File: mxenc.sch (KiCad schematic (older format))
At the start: 28 parts, among them J4 Conn_01x06, J6 Conn_01x06, J8 Conn_01x06 DNP, SW1 SW_Push, SW2 SW_Push, U1 IMX8MM, U10 24LC16, Y2 Crystal_GND24

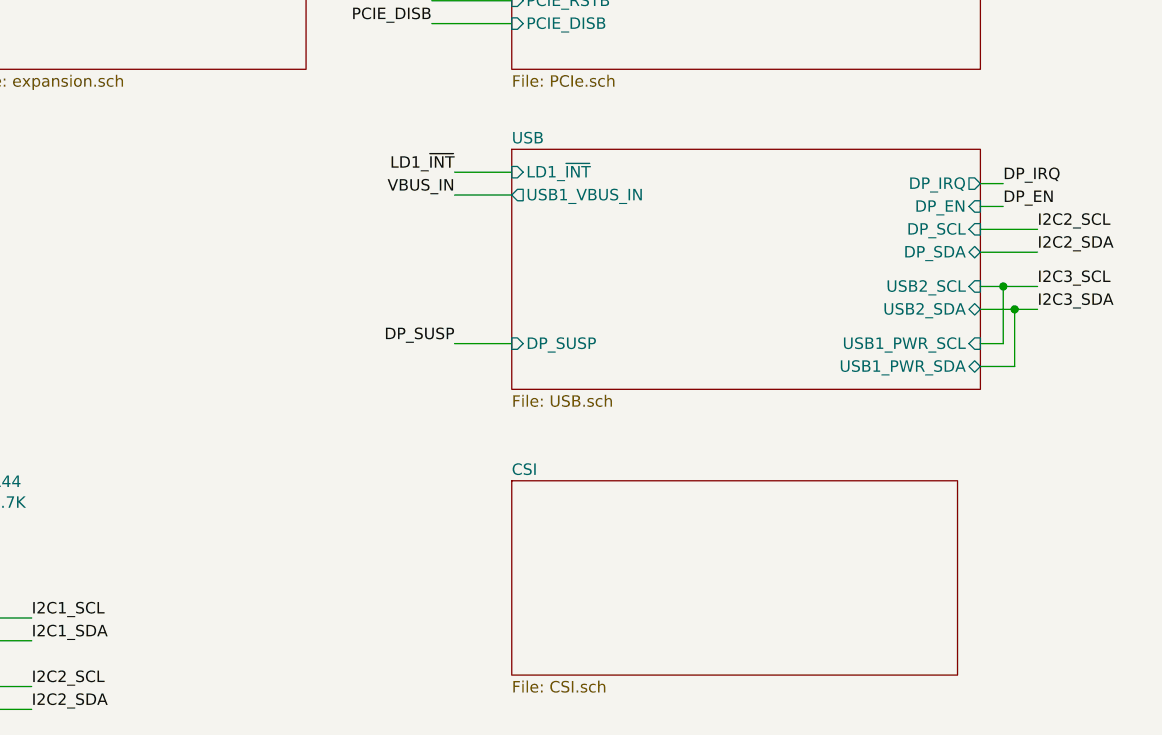
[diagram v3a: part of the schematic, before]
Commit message: UIM and USB routing for PCIE to expansion
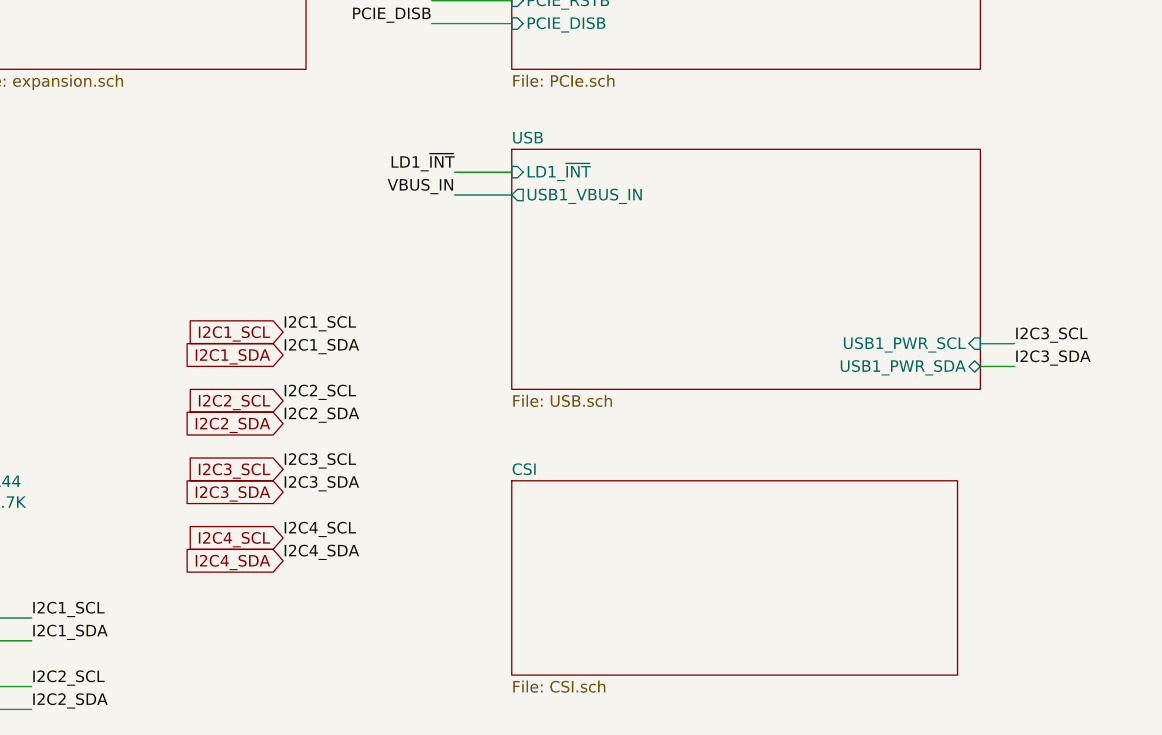
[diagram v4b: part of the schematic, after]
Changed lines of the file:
@@
-$EndSheet
-$Sheet
-S 13350 6750 2050 1050
-U 5D6742B7
-F0 "USB" 50
-F1 "USB.sch" 50
-F2 "LD1_~INT" I L 13350 6850 50
-F3 "USB1_VBUS_IN" O L 13350 6950 50
-F4 "DP_IRQ" O R 15400 6900 50
-F5 "DP_EN" I R 15400 7000 50
-F6 "DP_SCL" I R 15400 7100 50
-F7 "DP_SDA" B R 15400 7200 50
-F8 "USB2_SCL" I R 15400 7350 50
-F9 "USB2_SDA" B R 15400 7450 50
-F10 "USB1_PWR_SDA" B R 15400 7700 50
-F11 "USB1_PWR_SCL" I R 15400 7600 50
-F12 "DP_SUSP" I L 13350 7600 50
 $EndSheet
 $Sheet
@@
 Wire Wire Line
 	13100 6850 13350 6850
-Text Label 15500 7000 0    50   ~ 0
-DP_EN
-Wire Wire Line
-	15500 7000 15400 7000
-Text Label 15500 6900 0    50   ~ 0
-DP_IRQ
-Wire Wire Line
-	15500 6900 15400 6900
 Text Label 13000 5850 2    50   ~ 0
 I2C3_SDA
@@
 Text Label 1700 3350 0    50   ~ 0
 I2C2_SDA
-Text Label 15650 7350 0    50   ~ 0
+Text Label 15550 7600 0    50   ~ 0
 I2C3_SCL
-Text Label 15650 7450 0    50   ~ 0
-I2C3_SDA
-Wire Wire Line
-	15500 7350 15400 7350
-Wire Wire Line
-	15500 7350 15500 7600
-Wire Wire Line
-	15500 7600 15400 7600
-Wire Wire Line
-	15550 7450 15400 7450
-Wire Wire Line
-	15550 7450 15550 7700
+Wire Wire Line
+	15550 7600 15400 7600
 Wire Wire Line
 	15550 7700 15400 7700
-Text Label 13100 7600 2    50   ~ 0
-DP_SUSP
-Wire Wire Line
-	13100 7600 13350 7600
 Wire Wire Line
 	10600 1450 11000 1450
@@
 Text Notes 6200 3350 0    35   ~ 0
 WDOG - input, internal pull-up\nnINT - input, internal pull-up\nVSEL - output, 1.8v push-pull
-Wire Wire Line
-	15400 7100 15650 7100
-Wire Wire Line
-	15400 7200 15650 7200
-Wire Wire Line
-	15650 7350 15500 7350
-Connection ~ 15500 7350
-Wire Wire Line
-	15550 7450 15650 7450
-Connection ~ 15550 7450
 $Comp
 L mxenc:VDD_3V3 #PWR0142
@@
 	10600 7850 10600 7950
 Connection ~ 10600 7950
-Text Label 15650 7100 0    50   ~ 0
-I2C2_SCL
-Text Label 15650 7200 0    50   ~ 0
-I2C2_SDA
 $Comp
 L mxenc:GG_LOGO L8
@@
 ECSPI1_SS0
 $Comp
-L power:GND #PWR?
+L power:GND #PWR0217
 U 1 1 5F2A80D8
 P 2400 1450
-F 0 "#PWR?" H 2400 1200 50  0001 C CNN
+F 0 "#PWR0217" H 2400 1200 50  0001 C CNN
 F 1 "GND" H 2405 1277 50  0000 C CNN
 F 2 "" H 2400 1450 50  0001 C CNN
@@
 $EndComp
 $Comp
-L power:GND #PWR?
+L power:GND #PWR0218
 U 1 1 5F2A97FE
 P 3850 1450
-F 0 "#PWR?" H 3850 1200 50  0001 C CNN
+F 0 "#PWR0218" H 3850 1200 50  0001 C CNN
 F 1 "GND" H 3855 1277 50  0000 C CNN
 F 2 "" H 3850 1450 50  0001 C CNN
@@
 	1    0    0    -1
 $EndComp
+$Sheet
+S 13350 6750 2050 1050
+U 5D6742B7
+F0 "USB" 50
+F1 "USB.sch" 50
+F2 "LD1_~INT" I L 13350 6850 50
+F3 "USB1_VBUS_IN" O L 13350 6950 50
+F10 "USB1_PWR_SDA" B R 15400 7700 50
+F11 "USB1_PWR_SCL" I R 15400 7600 50
+$EndSheet
+Text Label 15550 7700 0    50   ~ 0
+I2C3_SDA
+Text Label 12350 8550 0    50   ~ 0
+I2C4_SDA
+Text Label 12350 8450 0    50   ~ 0
+I2C4_SCL
+Text Label 12350 8250 0    50   ~ 0
+I2C3_SDA
+Text Label 12350 8150 0    50   ~ 0
+I2C3_SCL
+Text Label 12350 7950 0    50   ~ 0
+I2C2_SDA
+Text Label 12350 7850 0    50   ~ 0
+I2C2_SCL
+Text Label 12350 7650 0    50   ~ 0
+I2C1_SDA
+Text Label 12350 7550 0    50   ~ 0
+I2C1_SCL
+Text GLabel 12350 7550 0    50   Input ~ 0
+I2C1_SCL
+Text GLabel 12350 7650 0    50   Input ~ 0
+I2C1_SDA
+Text GLabel 12350 7950 0    50   Input ~ 0
+I2C2_SDA
+Text GLabel 12350 8250 0    50   Input ~ 0
+I2C3_SDA
+Text GLabel 12350 8550 0    50   Input ~ 0
+I2C4_SDA
+Text GLabel 12350 7850 0    50   Input ~ 0
+I2C2_SCL
+Text GLabel 12350 8150 0    50   Input ~ 0
+I2C3_SCL
+Text GLabel 12350 8450 0    50   Input ~ 0
+I2C4_SCL
 $EndSCHEMATC

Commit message: Finish remaining routing
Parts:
- removed J8: Conn_01x06 DNP, Connector_PinHeader_2.54mm:PinHeader_1x06_P2.54mm_Horizontal, symbol Connector_Generic:Conn_01x06
- added J8: Conn_01x04_MountingPin, Connector_JST:JST_SH_SM04B-SRSS-TB_1x04-1MP_P1.00mm_Horizontal, symbol Connector_Generic_MountingPin:Conn_01x04_MountingPin
- added LOGO1: Logo_Open_Hardware_Small, Symbol:OSHW-Logo_5.7x6mm_SilkScreen, symbol Graphic:Logo_Open_Hardware_Small
- added R23, R38: 10K, Resistor_SMD:R_0201_0603Metric, symbol Device:R
- J4, J6: footprint Connector_JST:JST_GH_SM06B-GHS-TB_1x06-1MP_P1.25mm_Horizontal -> Connector_JST:JST_SH_SM06B-SRSS-TB_1x06-1MP_P1.00mm_Horizontal; symbol mxenc:JST-GH-6 -> Connector_Generic_MountingPin:Conn_01x06_MountingPin; Part SM06B-GHS-TB(LF)(SN) -> SM06B-SRSS-TB(LF)(SN); Vendorpart 455-1568-1-ND -> 455-1806-1-ND
- SW1, SW2: footprint mxenc:SW_SPST_EVQP7C -> mxenc:SW_SPST_EVQP7A
- U10: value 24LC16 -> 24C32; Mfgr Microchip -> ST; Part 24LC16B-I/MC -> M24C32-FMC6TG; Vendorpart 24LC16B-I/MC-ND -> 497-15757-1-ND
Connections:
- net VDD_5V is gone; now on net NVCC_3V3: J4.1 (Pin_1), J6.1 (Pin_1)
- net GND: now also J8.1 (Pin_1), J8.MP (MountPin), R38.1
- net I2C2_SCL: no longer U10.6 (SCL)
- net I2C2_SDA: no longer U10.5 (SDA)
- net I2C3_SCL: now also U10.6 (SCL)
- net I2C3_SDA: now also U10.5 (SDA)
- net I2C4_SCL: now also J8.4 (Pin_4)
- net I2C4_SDA: now also J8.3 (Pin_3)
- net JTAG_TRST_B: now also R23.1
- net UART1_CTS_B: no longer J6.4 (Pin_4)
- net UART1_RTS_B: no longer J6.5 (Pin_5)
- net UART1_RX: no longer J6.2 (Pin_2)
- net UART1_TX: no longer J6.3 (Pin_3)
- net VDD_1V8: now also R23.2; no longer U10.8 (VCC)
- net UART4_RX: now reaches U1.F19 (UART4_RXD/GPIO5[28])
- net UART4_RX: now also J6.2 (Pin_2)
- net NVCC_3V3: now reaches U10.1 (A0)
- net NVCC_3V3: now also U10.2 (A1), U10.3 (A2), U10.8 (VCC), J8.2 (Pin_2)
- net JTAG_MOD: no longer names the net of U1.D27 (JTAG_MOD)
- net JTAG_MOD: now also R38.2
- net LD1_~INT renamed UART4_TX
- net UART4_TX: now also J6.3 (Pin_3)
- new net UART4_CTS_B: J6.4 (Pin_4)
- new net UART4_RTS_B: J6.5 (Pin_5)
- no-connect marks 19 -> 14
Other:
- note added: "7-bit addr: 0x57/0x5F"
- note added: "CONSOLE (Pixhawk debug JST-SH)"
- note added: "I2C (QWIIC JST-SH)"
- note added: "UART1 (Pixhawk debug JST-SH)"
- note removed: "CONSOLE (0.1" connector)"
- note removed: "CONSOLE (JST connector)"
- note removed: "UART1 (JST connector)"
- moved on the sheet: L8

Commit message: wip more uart routing
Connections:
- net UART1_RX: now also U1.E14 (UART1_RXD); no longer U1.AB22 (SAI2_RXC/GPIO4[22]/UART1_RX)
- net UART1_TX: now also U1.F13 (UART1_TXD); no longer U1.AC19 (SAI2_RXFS/GPIO4[21]/UART1_TX)
- net UART2_RX: now also U1.F15 (UART2_RXD)
- net UART2_TX: now also U1.E15 (UART2_TXD)
- net UART3_TX: now reaches U1.D18 (UART3_TXD)
- net UART3_RX: now reaches U1.E18 (UART3_RXD)
- net GPIO1[11]: now reaches U1.AC10 (GPIO1_IO11)
- net GPIO1[9]: now reaches U1.AF10 (GPIO1_IO09)
- net UART1_CTS_B: no longer names the net of U1.AD23 (SAI2_TXFS/GPIO4[24]/UART1_CTS_B)
- net UART1_RTS_B: no longer names the net of U1.AC24 (SAI2_RXD0/GPIO4[23]/UART1_RTS_B)
- net USB2_OC renamed GPIO1[15]
- net USB2_PWR_EN renamed GPIO1[14]
- no-connect marks 14 -> 11
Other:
- note added: "A53 debug / UART2 (JST-SH)"
- note added: "M4 debug / UART4 (JST-SH)"
- note added: "QWIIC / I2C4 (JST-SH)"
- note removed: "CONSOLE (Pixhawk debug JST-SH)"
- note removed: "I2C (QWIIC JST-SH)"
- note removed: "UART1 (Pixhawk debug JST-SH)"
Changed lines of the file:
@@
 	1    0    0    -1
 $EndComp
-Wire Wire Line
-	6150 4900 6400 4900
-Wire Wire Line
-	6150 5000 6400 5000
 $Comp
 L mxenc:VDD_1V8 #PWR0246
@@
 Text Label 6450 1700 2    50   ~ 0
 LED_B
-Text Label 7900 2400 2    50   ~ 0
+Text Label 7300 9200 2    50   ~ 0
 UART2_TX
-Text Label 7900 2500 2    50   ~ 0
+Text Label 7300 9100 2    50   ~ 0
 UART2_RX
 Text Label 7900 2600 2    50   ~ 0
@@
 Text Label 7900 2700 2    50   ~ 0
 UART2_CTS_B
-Text Label 7900 3150 2    50   ~ 0
-UART1_TX
-Text Label 7900 3050 2    50   ~ 0
-UART1_RX
-Text Label 7900 2950 2    50   ~ 0
-UART1_RTS_B
-Text Label 7900 2850 2    50   ~ 0
-UART1_CTS_B
 Text Label 3500 1400 2    50   ~ 0
 UART2_TX
@@
 $EndSheet
 Text Notes 3150 2200 0    50   ~ 0
-CONSOLE (Pixhawk debug JST-SH)
+A53 debug / UART2 (JST-SH)
 Text Notes 1650 2200 0    50   ~ 0
-UART1 (Pixhawk debug JST-SH)
+M4 debug / UART4 (JST-SH)
 Text Notes 800  7950 0    35   ~ 0
 From NXP ref design: Recommend to use external clock source,\nXTALO must be connected to NVCC_SNVS_1V8/2, or VDD_SNVS_0V8!
@@
 Text Label 11250 8800 0    50   ~ 0
 I2C1_SCL
-NoConn ~ 7300 8900
-NoConn ~ 7300 8800
 $Comp
 L mxenc:VDD_1V8 #PWR0225
@@
 	9750 1150 9950 1150
 NoConn ~ 5600 3750
-NoConn ~ 5600 3850
 $Comp
 L Switch:SW_Push SW2
@@
 Text GLabel 9650 1150 0    50   Input ~ 0
 BTN1
-Text Label 5600 4350 0    50   ~ 0
-USB2_OTG_PWR
-Text Label 5600 4450 0    50   ~ 0
-USB2_OTG_OC
-Text Label 6150 5000 2    50   ~ 0
-USB2_OTG_PWR
-Text Label 6150 4900 2    50   ~ 0
-USB2_OTG_OC
-Text GLabel 6400 4900 2    50   Input ~ 0
-USB2_OC
-Text GLabel 6400 5000 2    50   Input ~ 0
-USB2_PWR_EN
 Text GLabel 3050 3700 0    50   Input ~ 0
 ECSPI2_SCLK
@@
 $EndComp
 Text Notes 4600 2200 0    50   ~ 0
-I2C (QWIIC JST-SH)
+QWIIC / I2C4 (JST-SH)
 $Comp
 L mxenc:NVCC_3V3 #PWR0235
@@
 Text Label 7300 9800 2    50   ~ 0
 UART4_TX
-Text Label 6600 2600 2    50   ~ 0
-UART1_TX
-Text Label 6600 2500 2    50   ~ 0
-UART1_RX
-Text Label 6600 2400 2    50   ~ 0
-UART1_RTS_B
-Text Label 6600 2300 2    50   ~ 0
-UART1_CTS_B
-Text GLabel 6600 2300 2    50   Input ~ 0
-UART1_CTS_B
-Text GLabel 6600 2400 2    50   Input ~ 0
-UART1_RTS_B
-Text GLabel 6600 2500 2    50   Input ~ 0
-UART1_RX
-Text GLabel 6600 2600 2    50   Input ~ 0
-UART1_TX
 $Comp
 L Device:R R23
@@
 	1    0    0    -1
 $EndComp
+Text GLabel 5600 3850 2    50   Input ~ 0
+GPIO1[9]
+Text GLabel 5600 4050 2    50   Input ~ 0
+GPIO1[11]
+Text GLabel 5600 4350 2    50   Input ~ 0
+GPIO1[14]
+Text GLabel 5600 4450 2    50   Input ~ 0
+GPIO1[15]
+Text GLabel 7300 8800 0    50   Input ~ 0
+UART1_RX
+Text GLabel 7300 8900 0    50   Input ~ 0
+UART1_TX
+Text GLabel 7300 9400 0    50   Input ~ 0
+UART3_RX
+Text GLabel 7300 9500 0    50   Input ~ 0
+UART3_TX
 $EndSCHEMATC

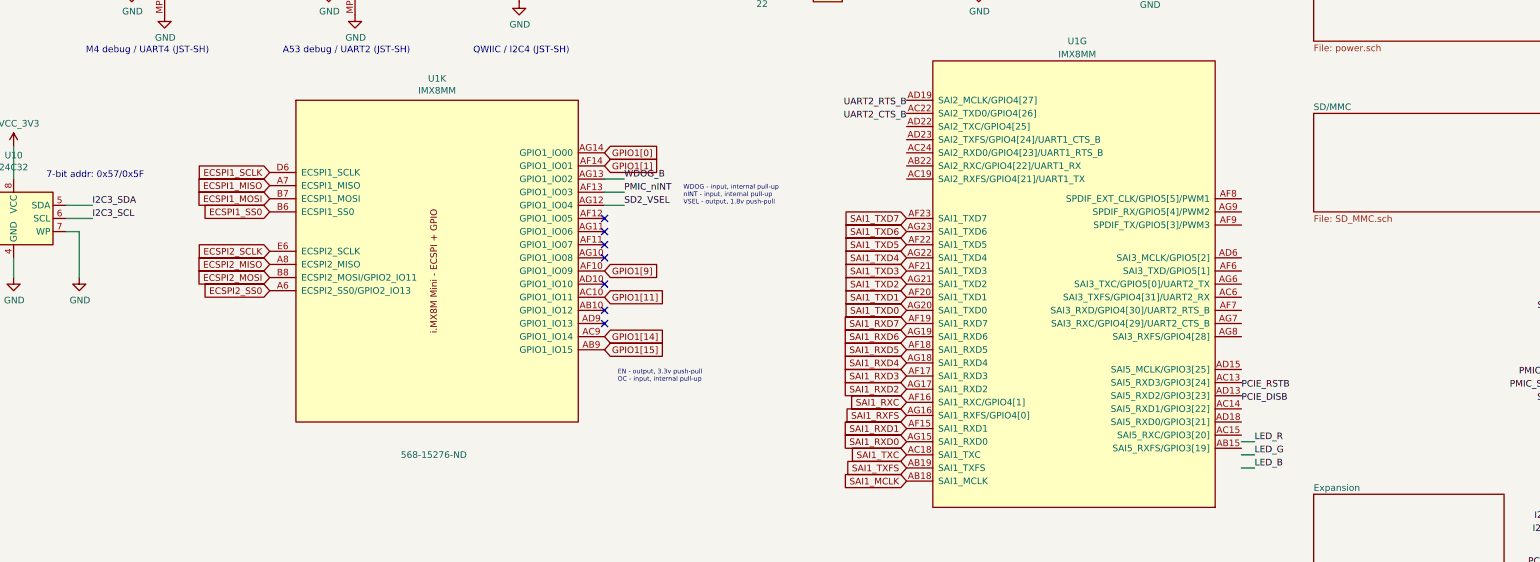
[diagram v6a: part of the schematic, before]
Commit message: prior to rerouting sai lanes
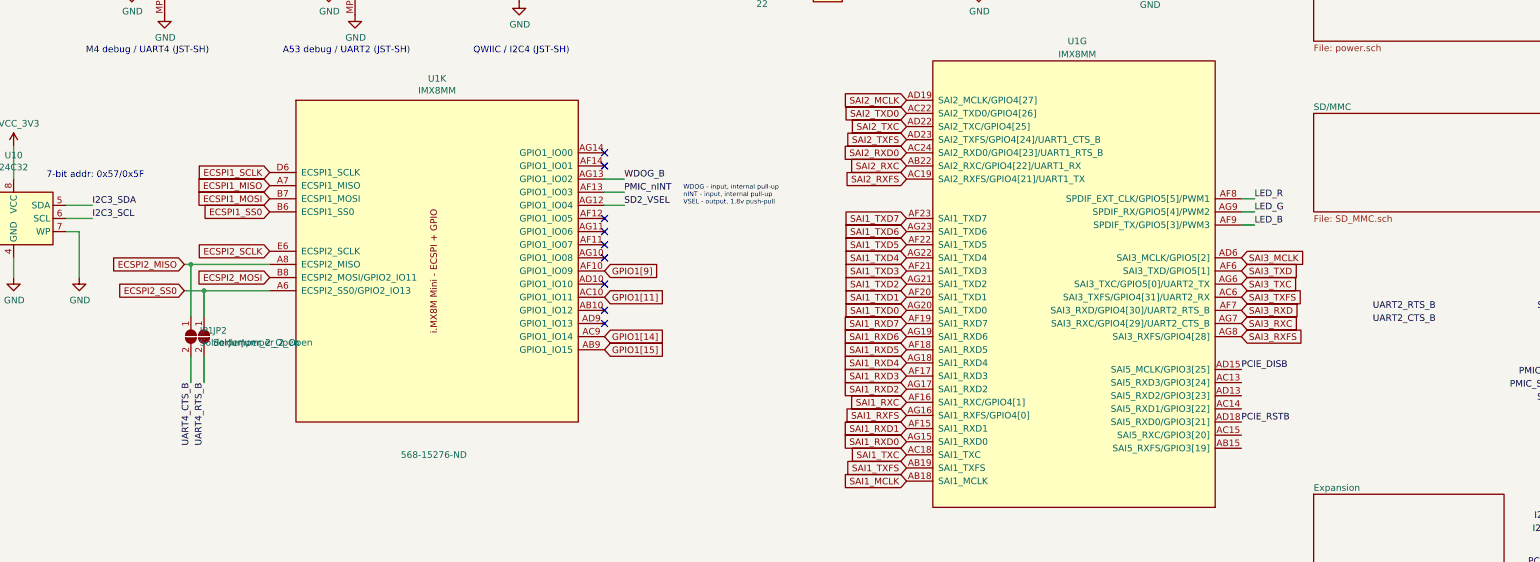
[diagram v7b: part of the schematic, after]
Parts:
- added JP1, JP2: SolderJumper_2_Open, Jumper:SolderJumper-2_P1.3mm_Open_TrianglePad1.0x1.5mm, symbol Jumper:SolderJumper_2_Open
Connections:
- net ECSPI2_MISO: now also JP1.1 (A)
- net ECSPI2_SS0: now also JP2.1 (A)
- net LED_B: now also U1.AF9 (SPDIF_TX/GPIO5[3]/PWM3)
- net LED_G: now also U1.AG9 (SPDIF_RX/GPIO5[4]/PWM2)
- net LED_R: now also U1.AF8 (SPDIF_EXT_CLK/GPIO5[5]/PWM1)
- net PCIE_DISB: now also U1.AD15 (SAI5_MCLK/GPIO3[25])
- net PCIE_RSTB: now also U1.AD18 (SAI5_RXD0/GPIO3[21])
- net UART4_CTS_B: now also JP1.2 (B)
- net UART4_RTS_B: now also JP2.2 (B)
- net SAI2_RXC: now reaches U1.AB22 (SAI2_RXC/GPIO4[22]/UART1_RX)
- net SAI2_RXFS: now reaches U1.AC19 (SAI2_RXFS/GPIO4[21]/UART1_TX)
- net SAI2_TXD0: now reaches U1.AC22 (SAI2_TXD0/GPIO4[26])
- net SAI2_RXD0: now reaches U1.AC24 (SAI2_RXD0/GPIO4[23]/UART1_RTS_B)
- net SAI3_TXFS: now reaches U1.AC6 (SAI3_TXFS/GPIO4[31]/UART2_RX)
- net SAI2_MCLK: now reaches U1.AD19 (SAI2_MCLK/GPIO4[27])
- net SAI2_TXC: now reaches U1.AD22 (SAI2_TXC/GPIO4[25])
- net SAI2_TXFS: now reaches U1.AD23 (SAI2_TXFS/GPIO4[24]/UART1_CTS_B)
- net SAI3_MCLK: now reaches U1.AD6 (SAI3_MCLK/GPIO5[2])
- net SAI3_TXD: now reaches U1.AF6 (SAI3_TXD/GPIO5[1])
- net SAI3_RXD: now reaches U1.AF7 (SAI3_RXD/GPIO4[30]/UART2_RTS_B)
- net SAI3_TXC: now reaches U1.AG6 (SAI3_TXC/GPIO5[0]/UART2_TX)
- net SAI3_RXC: now reaches U1.AG7 (SAI3_RXC/GPIO4[29]/UART2_CTS_B)
- net SAI3_RXFS: now reaches U1.AG8 (SAI3_RXFS/GPIO4[28])
- net GPIO1[0]: no longer names the net of U1.AG14 (GPIO1_IO00)
- net GPIO1[1]: no longer names the net of U1.AF14 (GPIO1_IO01)
- no-connect marks 11 -> 13
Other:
- note removed: "EN - output, 3.3v push-pull\nOC - input, internal pull-up"
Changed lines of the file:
@@
 $EndComp
 Wire Wire Line
-	10450 5350 10550 5350
-Wire Wire Line
-	10450 5250 10550 5250
+	10450 3500 10550 3500
+Wire Wire Line
+	10450 3400 10550 3400
 $Comp
 L mxenc:VDD_3V3 #PWR0250
@@
 Wire Wire Line
 	6650 1300 6450 1300
-Text Label 10550 5150 0    50   ~ 0
+Text Label 10550 3300 0    50   ~ 0
 LED_R
-Text Label 10550 5250 0    50   ~ 0
+Text Label 10550 3400 0    50   ~ 0
 LED_G
-Text Label 10550 5350 0    50   ~ 0
+Text Label 10550 3500 0    50   ~ 0
 LED_B
 $Comp
@@
 $EndComp
 Wire Wire Line
-	10450 5150 10550 5150
+	10450 3300 10550 3300
 Text Label 6450 1300 2    50   ~ 0
 LED_R
@@
 Text Label 7300 9100 2    50   ~ 0
 UART2_RX
-Text Label 7900 2600 2    50   ~ 0
+Text Label 11450 4150 0    50   ~ 0
 UART2_RTS_B
-Text Label 7900 2700 2    50   ~ 0
+Text Label 11450 4250 0    50   ~ 0
 UART2_CTS_B
 Text Label 3500 1400 2    50   ~ 0
@@
 Wire Wire Line
 	13000 6200 13350 6200
-Text Label 10450 4750 0    50   ~ 0
+Text Label 10450 5000 0    50   ~ 0
 PCIE_RSTB
-Text Label 10450 4850 0    50   ~ 0
+Text Label 10450 4600 0    50   ~ 0
 PCIE_DISB
 Text Label 13100 6850 2    50   ~ 0
@@
 Text Label 6000 6600 0    50   ~ 0
 BTN0
-Text Notes 5700 4700 0    35   ~ 0
-EN - output, 3.3v push-pull\nOC - input, internal pull-up
 Text Notes 6200 3350 0    35   ~ 0
 WDOG - input, internal pull-up\nnINT - input, internal pull-up\nVSEL - output, 1.8v push-pull
@@
 	1    0    0    -1
 $EndComp
-Text GLabel 5600 2950 2    50   Input ~ 0
-GPIO1[0]
-Text GLabel 5600 3050 2    50   Input ~ 0
-GPIO1[1]
 Text GLabel 7900 3450 0    50   Input ~ 0
 SAI1_TXD7
@@
 Text GLabel 3050 3700 0    50   Input ~ 0
 ECSPI2_SCLK
-Text GLabel 3050 3800 0    50   Input ~ 0
+Text GLabel 2400 3800 0    50   Input ~ 0
 ECSPI2_MISO
 Text GLabel 3050 3900 0    50   Input ~ 0
 ECSPI2_MOSI
-Text GLabel 3050 4000 0    50   Input ~ 0
+Text GLabel 2400 4000 0    50   Input ~ 0
 ECSPI2_SS0
 Text GLabel 3050 3100 0    50   Input ~ 0
@@
 Text GLabel 7300 9500 0    50   Input ~ 0
 UART3_TX
+Wire Wire Line
+	2400 3800 2450 3800
+Wire Wire Line
+	2400 4000 2550 4000
+$Comp
+L Jumper:SolderJumper_2_Open JP1
+U 1 1 5F026C85
+P 2450 4350
+F 0 "JP1" V 2404 4418 50  0000 L CNN
+F 1 "SolderJumper_2_Open" V 2495 4418 50  0000 L CNN
+F 2 "Jumper:SolderJumper-2_P1.3mm_Open_TrianglePad1.0x1.5mm" H 2450 4350 50  0001 C CNN
+F 3 "~" H 2450 4350 50  0001 C CNN
+	1    2450 4350
+	0    1    1    0
+$EndComp
+$Comp
+L Jumper:SolderJumper_2_Open JP2
+U 1 1 5F027943
+P 2550 4350
+F 0 "JP2" V 2504 4418 50  0000 L CNN
+F 1 "SolderJumper_2_Open" V 2595 4418 50  0000 L CNN
+F 2 "Jumper:SolderJumper-2_P1.3mm_Open_TrianglePad1.0x1.5mm" H 2550 4350 50  0001 C CNN
+F 3 "~" H 2550 4350 50  0001 C CNN
+	1    2550 4350
+	0    1    1    0
+$EndComp
+Wire Wire Line
+	2450 3800 2450 4200
+Connection ~ 2450 3800
+Wire Wire Line
+	2450 3800 3050 3800
+Wire Wire Line
+	2550 4000 2550 4200
+Connection ~ 2550 4000
+Wire Wire Line
+	2550 4000 3050 4000
+Wire Wire Line
+	2450 4700 2450 4500
+Wire Wire Line
+	2550 4700 2550 4500
+Text Label 2450 4700 3    50   ~ 0
+UART4_CTS_B
+Text Label 2550 4700 3    50   ~ 0
+UART4_RTS_B
+NoConn ~ 5600 2950
+NoConn ~ 5600 3050
+Text GLabel 10450 3750 2    50   Input ~ 0
+SAI3_MCLK
+Text GLabel 10450 3850 2    50   Input ~ 0
+SAI3_TXD
+Text GLabel 10450 3950 2    50   Input ~ 0
+SAI3_TXC
+Text GLabel 10450 4050 2    50   Input ~ 0
+SAI3_TXFS
+Text GLabel 10450 4150 2    50   Input ~ 0
+SAI3_RXD
+Text GLabel 10450 4250 2    50   Input ~ 0
+SAI3_RXC
+Text GLabel 10450 4350 2    50   Input ~ 0
+SAI3_RXFS
+Text GLabel 7900 2550 0    50   Input ~ 0
+SAI2_MCLK
+Text GLabel 7900 2650 0    50   Input ~ 0
+SAI2_TXD0
+Text GLabel 7900 2750 0    50   Input ~ 0
+SAI2_TXC
+Text GLabel 7900 2850 0    50   Input ~ 0
+SAI2_TXFS
+Text GLabel 7900 2950 0    50   Input ~ 0
+SAI2_RXD0
+Text GLabel 7900 3050 0    50   Input ~ 0
+SAI2_RXC
+Text GLabel 7900 3150 0    50   Input ~ 0
+SAI2_RXFS
 $EndSCHEMATC
